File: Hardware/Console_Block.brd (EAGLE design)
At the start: 30.5 x 44.5 mm, 41 parts, among them Q1 BSS138, U2 FTS31XS-U, U4 TPS62065

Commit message: file cleanup
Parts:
- L1: value (none) -> 1.0uH
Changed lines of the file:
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@@
 <attribute name="PROD_ID" value="CAP-08280" x="4.826" y="9.271" size="1.778" layer="27" display="off"/>
 </element>
-<element name="L1" library="SparkFun-Passives" package="INDUCTOR-SRP4020" value="" x="14.986" y="18.796"/>
+<element name="L1" library="SparkFun-Passives" package="INDUCTOR-SRP4020" value="1.0uH" x="14.986" y="18.796"/>
 <element name="LOGO1" library="SparkFun-Aesthetics" package="SFE_LOGO_NAME_FLAME_.1" value="SFE_LOGO_NAME_FLAME.1_INCH" x="9.271" y="0.254"/>
 <element name="LOGO4" library="SparkFun-Aesthetics" package="OSHW-LOGO-S" value="OSHW-LOGOS" x="5.842" y="1.778"/>
@@
 <contactref element="U$3" pad="27"/>
 <contactref element="R7" pad="2"/>
-<wire x1="24.765" y1="23.241" x2="24.765" y2="18.161" width="0.1524" layer="1"/>
+<wire x1="24.765" y1="23.749" x2="24.765" y2="18.161" width="0.1524" layer="1"/>
 <wire x1="24.765" y1="18.161" x2="25.1462" y2="17.7798" width="0.1524" layer="1"/>
 <wire x1="25.96" y1="17.7798" x2="25.1462" y2="17.7798" width="0.1524" layer="1"/>
-<wire x1="24.765" y1="23.241" x2="22.86" y2="25.146" width="0.1524" layer="1"/>
+<wire x1="24.765" y1="23.749" x2="23.368" y2="25.146" width="0.1524" layer="1"/>
 <wire x1="19.558" y1="26.328" x2="19.558" y2="25.4" width="0.1524" layer="1"/>
 <wire x1="19.558" y1="25.4" x2="19.812" y2="25.146" width="0.1524" layer="1"/>
-<wire x1="19.812" y1="25.146" x2="22.86" y2="25.146" width="0.1524" layer="1"/>
+<wire x1="19.812" y1="25.146" x2="23.368" y2="25.146" width="0.1524" layer="1"/>
 </signal>
 <signal name="GP134_UART_2_RX">
@@
 <contactref element="U$3" pad="22"/>
 <contactref element="R6" pad="2"/>
-<wire x1="22.86" y1="24.638" x2="24.384" y2="23.114" width="0.1524" layer="1"/>
-<wire x1="24.384" y1="23.114" x2="24.384" y2="19.304" width="0.1524" layer="1"/>
+<wire x1="23.368" y1="24.638" x2="24.384" y2="23.622" width="0.1524" layer="1"/>
+<wire x1="24.384" y1="23.622" x2="24.384" y2="19.304" width="0.1524" layer="1"/>
 <wire x1="24.384" y1="19.304" x2="24.0598" y2="18.9798" width="0.1524" layer="1"/>
 <wire x1="23.32" y1="18.9798" x2="24.0598" y2="18.9798" width="0.1524" layer="1"/>
-<wire x1="22.86" y1="24.638" x2="16.344" y2="24.638" width="0.1524" layer="1"/>
+<wire x1="23.368" y1="24.638" x2="16.344" y2="24.638" width="0.1524" layer="1"/>
 </signal>
 <signal name="GP43_I2S_2_TXD">

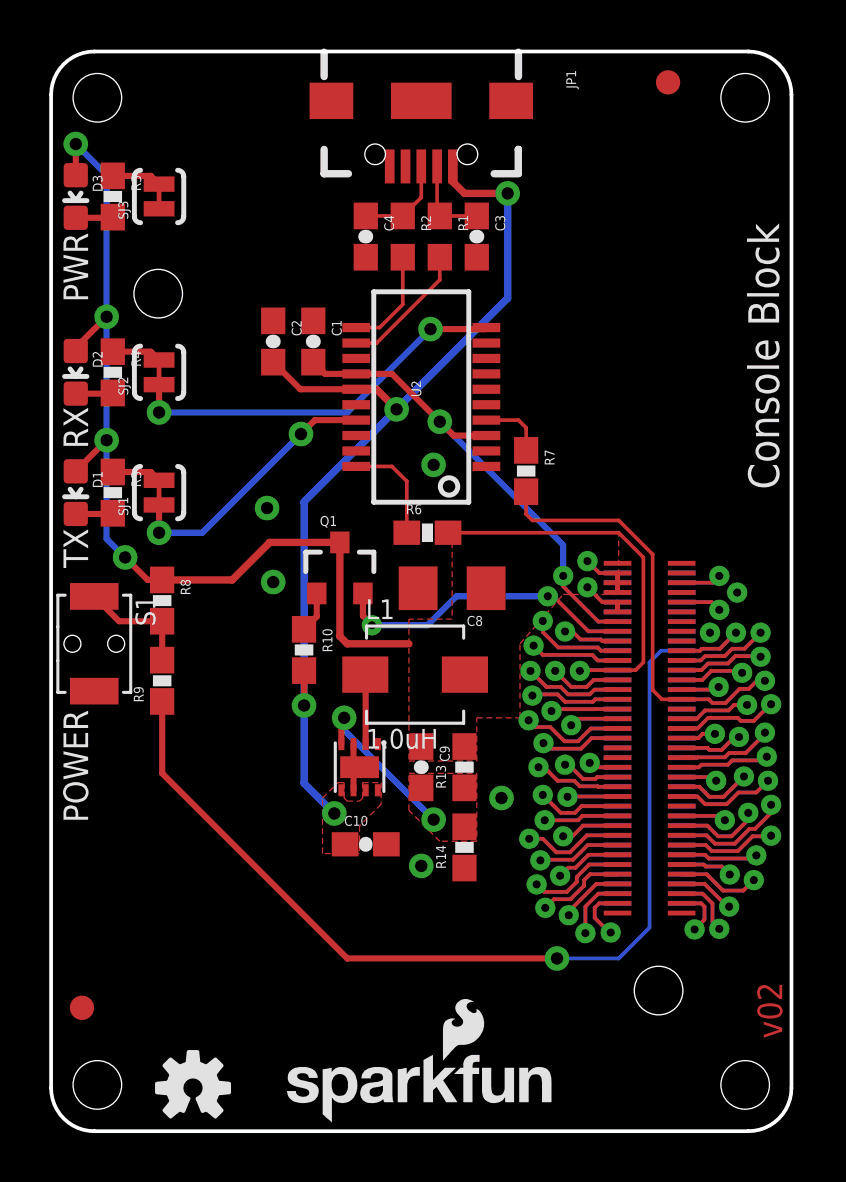
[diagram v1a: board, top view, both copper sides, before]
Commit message: changed rev number to v01 replaced ouput capacitor on vreg to 22uF replaced filter capacitor on vreg to 47pf replaced connector footprints to add T/Brestrict to prevent solder bridging
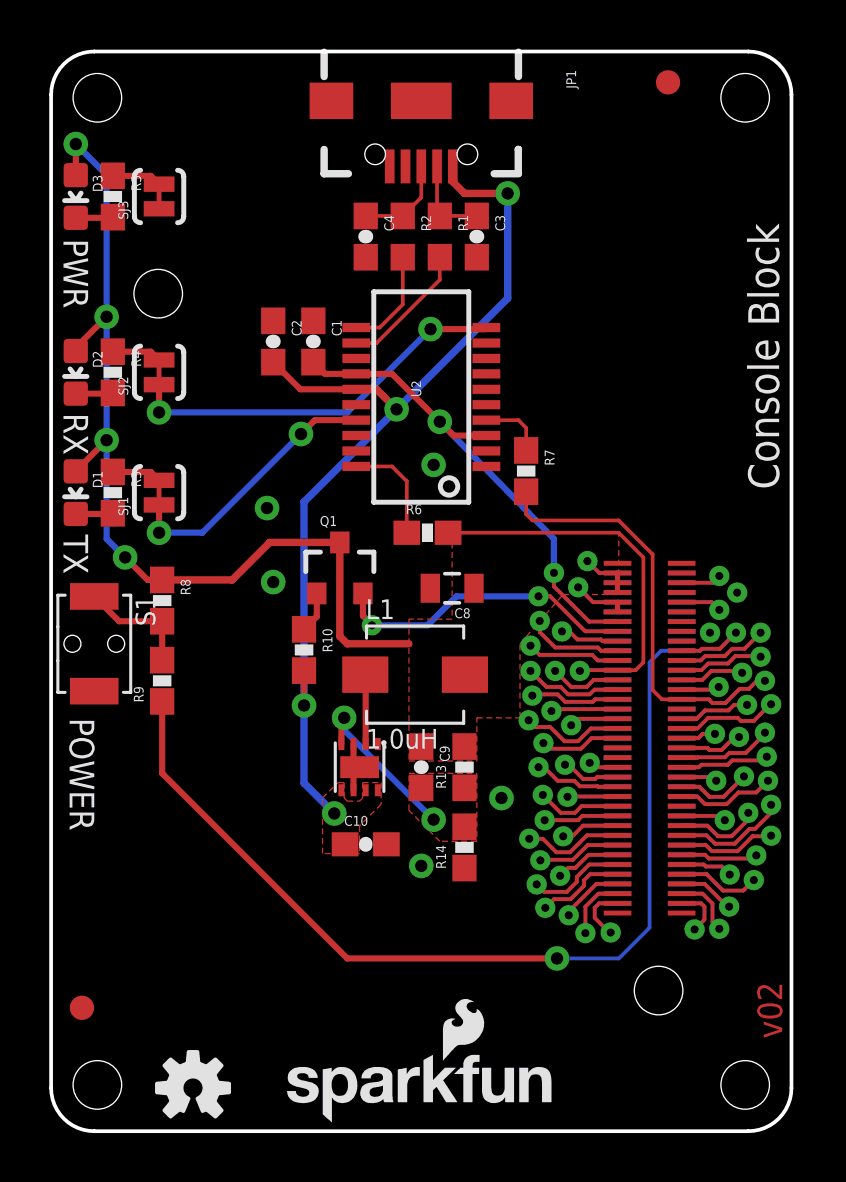
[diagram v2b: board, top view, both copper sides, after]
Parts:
- C8: value 10uF -> 22uF; device SparkFun-Capacitors:1206 -> SparkFun-Capacitors:0805
- C9: value 22pF -> 47pF
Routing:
- net 3.3V: track 3.99 -> 4.75 mm
- net 1.8V: track 23.4 -> 24.1 mm

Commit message: fixed bridging
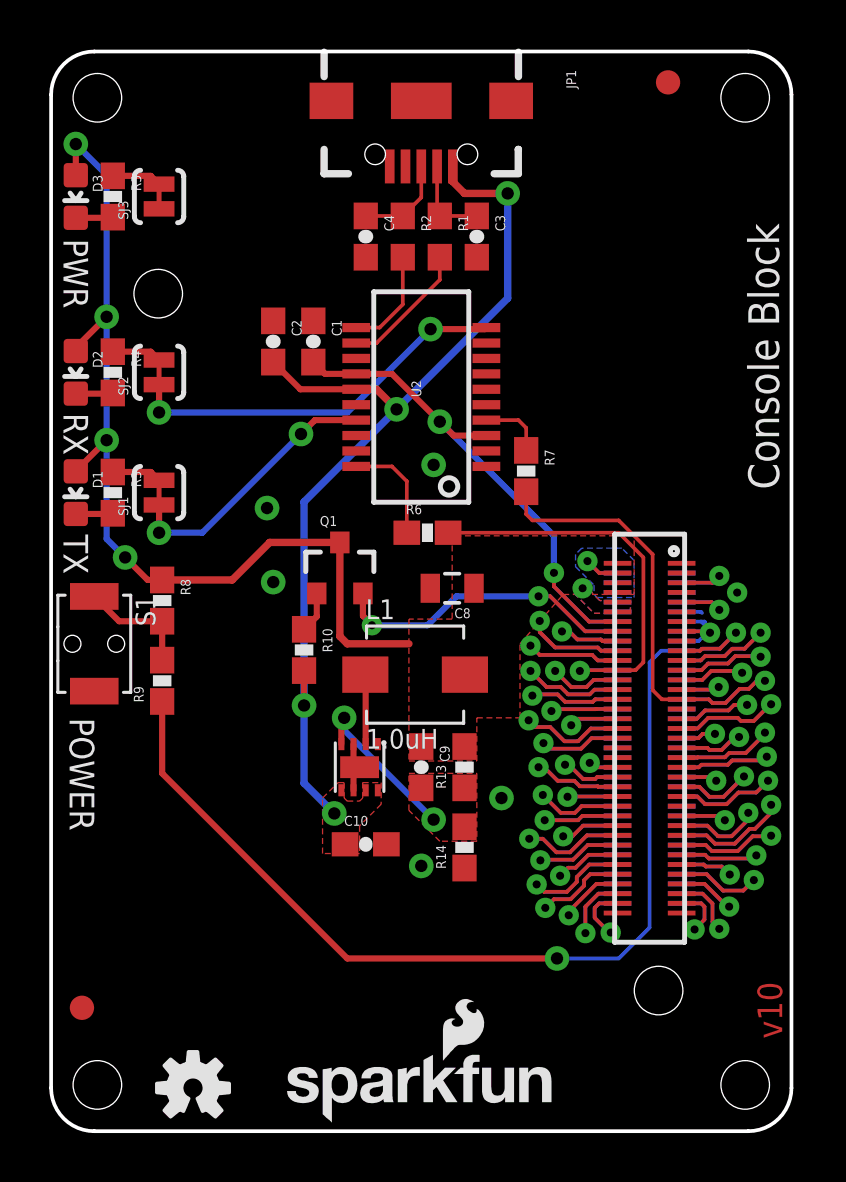
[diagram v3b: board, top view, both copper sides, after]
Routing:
- net GND: track 2.11 -> 7.16 mm
- net 3.3V: track 4.75 -> 0.00 mm
- net VSYS: track 44.4 -> 42.8 mm
- added copper zone on layer 1, net 3.3V
- added copper zone on layer 16, net 3.3V
- added copper zone on layer 16, net VSYS
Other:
- board text added: "v10"
- board text removed: "v02"

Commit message: added ground vias to solidify ground planes. also added staking vias for USB connectors.
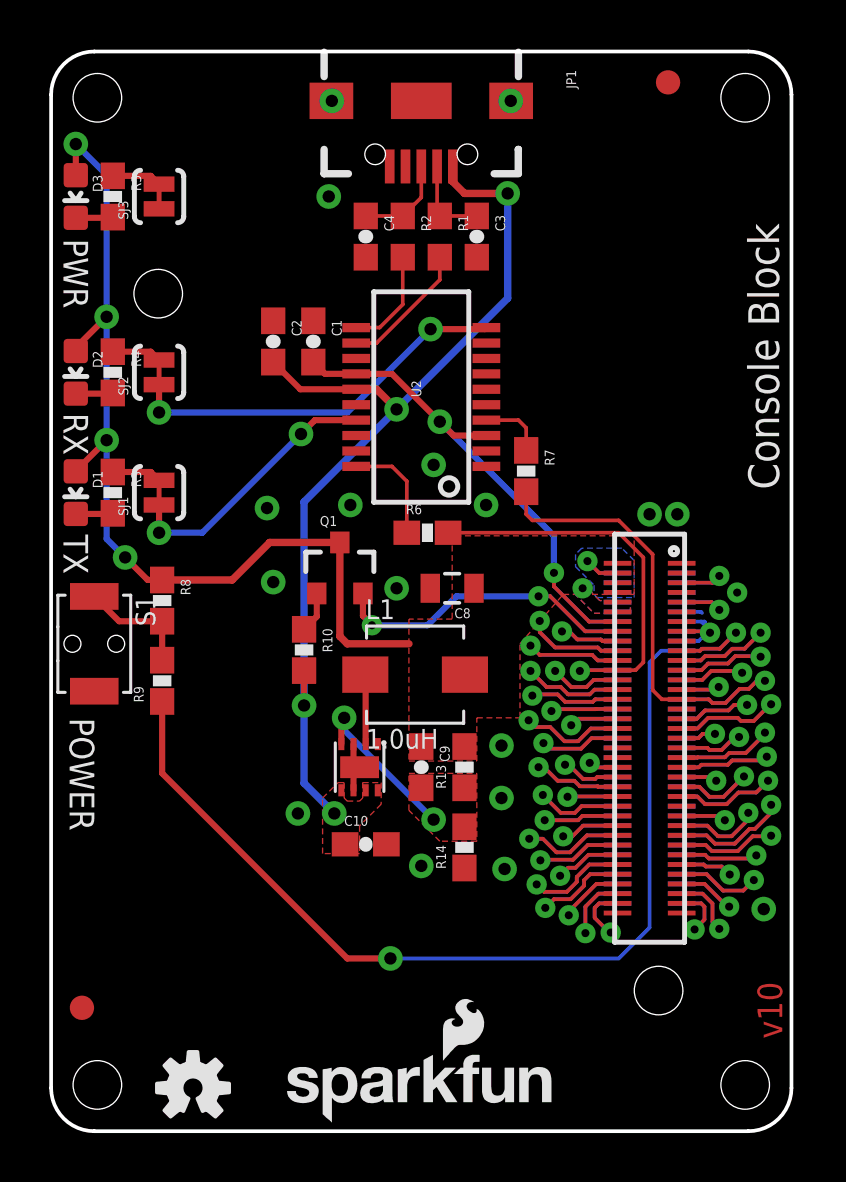
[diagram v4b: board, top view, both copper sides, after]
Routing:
- net GND: vias 7 -> 19

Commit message: Add a couple vias near FTDI for gnd
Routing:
- net GND: vias 19 -> 21

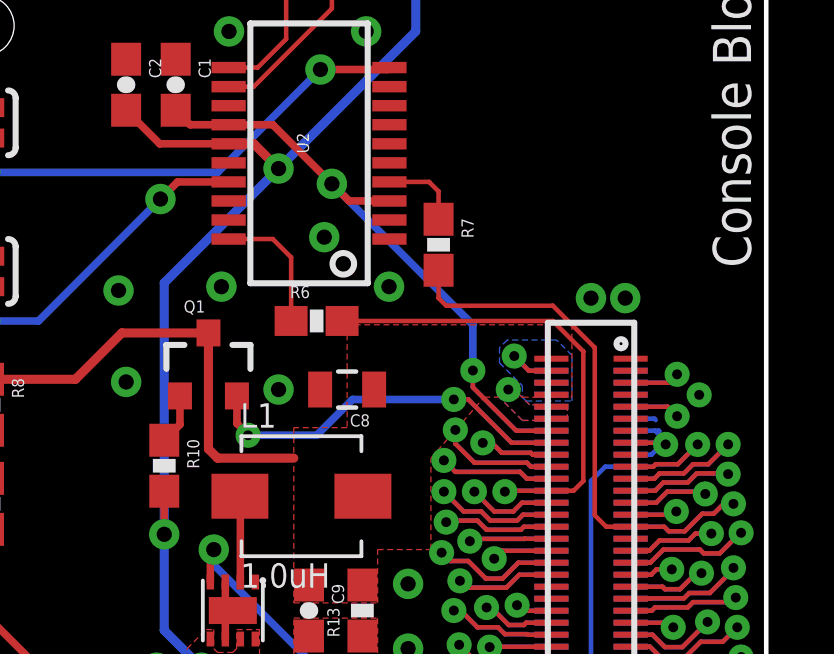
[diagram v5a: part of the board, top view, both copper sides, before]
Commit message: fixed footprint
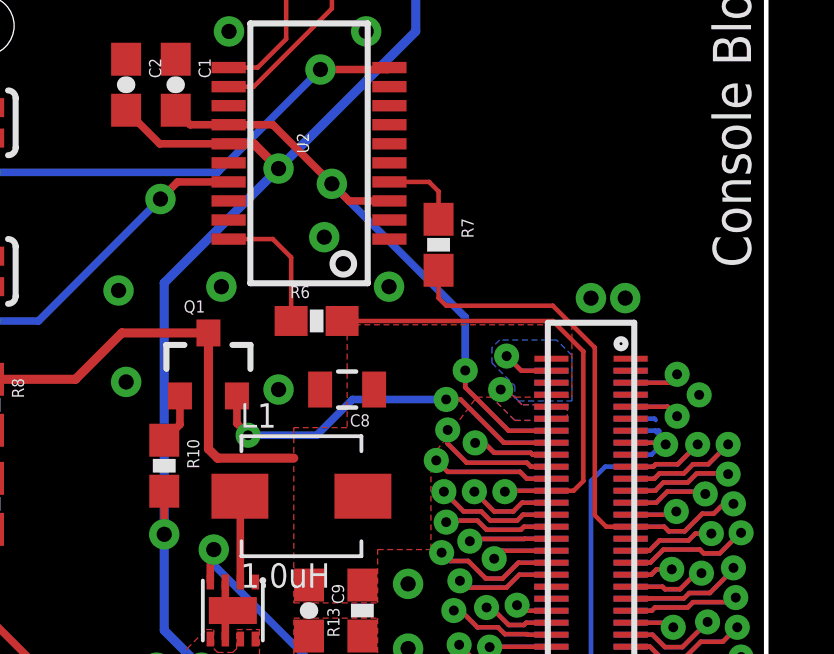
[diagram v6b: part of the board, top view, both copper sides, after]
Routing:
- net USB_VBUS: track 7.67 -> 8.18 mm
- net USB_DN: track 7.96 -> 8.47 mm
- net USB_DP: track 4.90 -> 5.41 mm
- net VSYS: track 42.8 -> 43.3 mm
